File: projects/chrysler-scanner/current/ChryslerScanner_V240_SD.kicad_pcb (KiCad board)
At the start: 4 copper layers, 110 x 55 mm, 281 parts, among them J1 226A-1202, J2 USB-C, J3 I2C, J4 microSD / DM3AT-SF-PEJM5, Q1 CJ3439KDW, Q10 DMC3071LVT-7, Q11 DMC3071LVT-7, Q12 DMG6601LVT-7, Q13 DMG6601LVT-7, Q14 DMG6601LVT-7, Q15 DMG6601LVT-7, Q16 CJ3439KDW, Q17 AO3400, Q18 AO3400, Q19 AO3400, Q2 2N7002DW, Q20 AO3400, Q3 2N7002DW, Q4 2N7002DW, Q5 UMH3N, Q6 CJ3439KDW, Q7 HSSK8811, Q8 DMC3071LVT-7, Q9 DMC3071LVT-7, SW1 RESET, SW2 BOOT, SW3 LOG / SAFE STOP, U1 SY6283, U10 ESP32-PICO-V3-02, U11 USBLC6-2SC6, U12 CP2102, U13 74LVC2G66, U14 74LVC2G66, U15 74LVC2G66, U16 TS391C, U17 74LVC1G17, U18 74LVC1G14, U19 AW9523B, U2 LMR14010, U20 MCP1825S-3302E/DB, U21 TMUX1511PWR, U22 LTC6993HS6-2#TRMPBF, U23 SN74LVC1G11DBVR, U24 TLV803EA30DBZR, U3 TLV76750DRV, U4 TLV76733DRV, U5 LGS6302, U6 LMR14010, U7 LMR14010, U8 TLV76701DRV, U9 TS391C

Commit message: Add hook test points and mapped debug access with verified fabrication outputs
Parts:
- added TP1: J1962-16, footprints:TestPoint_Keystone_5015_Micro_Mini, F.Cu at (107.8, 143.6)
- added TP10: PCI_VCC, footprints:TestPoint_Keystone_5015_Micro_Mini, B.Cu at (119.5, 126.1)
- added TP11: J1962-2, footprints:TestPoint_Keystone_5015_Micro_Mini, B.Cu at (114.8, 119.3)
- added TP12: J1962-3, footprints:TestPoint_Keystone_5015_Micro_Mini, B.Cu at (119.5, 116.3)
- added TP13: J1962-11, footprints:TestPoint_Keystone_5015_Micro_Mini, B.Cu at (115.3, 115.2)
- added TP14: J1962-6, footprints:TestPoint_Keystone_5015_Micro_Mini, B.Cu at (142.7, 130.9)
- added TP15: J1962-12, footprints:TestPoint_Keystone_5015_Micro_Mini, B.Cu at (118.4, 138.3)
- added TP16: J1962-14, footprints:TestPoint_Keystone_5015_Micro_Mini, B.Cu at (163.0, 152.0)
- added TP17: J1962-9, footprints:TestPoint_Keystone_5015_Micro_Mini, F.Cu at (140.4, 142.8)
- added TP18: J1962-7, footprints:TestPoint_Keystone_5015_Micro_Mini, B.Cu at (128.8, 147.5)
- added TP19: J1962-15, footprints:TestPoint_Keystone_5015_Micro_Mini, B.Cu at (125.0, 150.4)
- added TP2: +12V, footprints:TestPoint_Keystone_5015_Micro_Mini, B.Cu at (110.6, 135.0)
- added TP20: TX0, footprints:TestPoint_Keystone_5015_Micro_Mini, B.Cu at (198.6, 119.3)
- added TP21: RX0, footprints:TestPoint_Keystone_5015_Micro_Mini, F.Cu at (187.5, 121.1)
- added TP22: EN, footprints:TestPoint_Keystone_5015_Micro_Mini, B.Cu at (157.2, 104.8)
- added TP23: IO0, footprints:TestPoint_Keystone_5015_Micro_Mini, F.Cu at (186.6, 149.7)
- added TP24: SCL, footprints:TestPoint_Keystone_5015_Micro_Mini, B.Cu at (175.3, 143.8)
- added TP25: SDA, footprints:TestPoint_Keystone_5015_Micro_Mini, F.Cu at (162.8, 118.6)
- added TP26: PCI_RX, footprints:TestPoint_Keystone_5015_Micro_Mini, B.Cu at (131.3, 121.0)
- added TP27: PCI_TX, footprints:TestPoint_Keystone_5015_Micro_Mini, B.Cu at (161.9, 125.8)
- added TP28: RX1, footprints:TestPoint_Keystone_5015_Micro_Mini, B.Cu at (171.5, 106.6)
- added TP29: TX1, footprints:TestPoint_Keystone_5015_Micro_Mini, B.Cu at (130.9, 104.4)
- added TP3: VBUS, footprints:TestPoint_Keystone_5015_Micro_Mini, B.Cu at (204.1, 110.5)
- added TP30: RX2, footprints:TestPoint_Keystone_5015_Micro_Mini, B.Cu at (136.1, 146.9)
- added TP31: TX2, footprints:TestPoint_Keystone_5015_Micro_Mini, B.Cu at (124.1, 139.2)
- added TP32: ACT_LED, footprints:TestPoint_Keystone_5015_Micro_Mini, B.Cu at (183.3, 122.3)
- added TP33: HEARTBEAT_VALID, footprints:TestPoint_Keystone_5015_Micro_Mini, B.Cu at (161.8, 105.0)
- added TP34: LOGIC_PG, footprints:TestPoint_Keystone_5015_Micro_Mini, B.Cu at (162.5, 145.8)
- added TP35: N_R88_2, footprints:TestPoint_Keystone_5015_Micro_Mini, B.Cu at (152.9, 126.7)
- added TP36: V_BA_PRE, footprints:TestPoint_Keystone_5015_Micro_Mini, B.Cu at (144.2, 113.2)
- added TP37: V_BA, footprints:TestPoint_Keystone_5015_Micro_Mini, B.Cu at (146.4, 126.7)
- added TP38: V_BT_PRE, footprints:TestPoint_Keystone_5015_Micro_Mini, B.Cu at (171.7, 129.1)
- added TP39: V_BT, footprints:TestPoint_Keystone_5015_Micro_Mini, B.Cu at (154.3, 150.6)
- added TP4: +5V, footprints:TestPoint_Keystone_5015_Micro_Mini, F.Cu at (130.1, 117.6)
- added TP40: V_PR_PRE, footprints:TestPoint_Keystone_5015_Micro_Mini, B.Cu at (139.3, 112.9)
- added TP41: V_PR, footprints:TestPoint_Keystone_5015_Micro_Mini, B.Cu at (167.0, 130.5)
- added TP42: SD_DETECT, footprints:TestPoint_Keystone_5015_Micro_Mini, F.Cu at (195.7, 139.3)
- added TP43: CCD+, footprints:TestPoint_Keystone_5015_Micro_Mini, F.Cu at (129.8, 112.8)
- added TP44: CCD-, footprints:TestPoint_Keystone_5015_Micro_Mini, B.Cu at (121.2, 111.8)
- added TP45: SD_CS, footprints:TestPoint_Pad_D1.0mm, B.Cu at (181.6, 133.3)
- added TP46: SD_SCK, footprints:TestPoint_Pad_D1.0mm, F.Cu at (191.6, 139.3)
- added TP47: SD_MOSI, footprints:TestPoint_Pad_D1.0mm, B.Cu at (184.4, 131.0)
- added TP48: SD_MISO, footprints:TestPoint_Pad_D1.0mm, B.Cu at (187.5, 113.4)
- added TP49: GND, footprints:TestPoint_Keystone_5015_Micro_Mini, B.Cu at (115.2, 143.0)
- added TP5: +3.3V, footprints:TestPoint_Keystone_5015_Micro_Mini, B.Cu at (159.9, 131.9)
- added TP50: GND, footprints:TestPoint_Keystone_5015_Micro_Mini, B.Cu at (134.4, 152.2)
- added TP51: GND, footprints:TestPoint_Keystone_5015_Micro_Mini, B.Cu at (169.3, 145.2)
- added TP52: GND, footprints:TestPoint_Keystone_5015_Micro_Mini, B.Cu at (204.0, 114.4)
- added TP6: SD_3V3, footprints:TestPoint_Keystone_5015_Micro_Mini, B.Cu at (199.0, 134.6)
- added TP7: +7.5V, footprints:TestPoint_Keystone_5015_Micro_Mini, B.Cu at (197.2, 112.1)
- added TP8: VBB, footprints:TestPoint_Keystone_5015_Micro_Mini, B.Cu at (138.3, 126.7)
- added TP9: VPP, footprints:TestPoint_Keystone_5015_Micro_Mini, F.Cu at (149.6, 125.9)
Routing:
- net TX0: track 2.43 -> 8.13 mm, vias 0 -> 1
- net SD_MOSI: track 29.4 -> 34.8 mm, vias 2 -> 3
- net HEARTBEAT_VALID: track 12.9 -> 18.1 mm, vias 2 -> 3
- net V_PR_PRE: track 60.3 -> 65.3 mm
- net IO0: track 56.6 -> 60.6 mm
- net SD_3V3: track 27.5 -> 30.5 mm
- net SCL: track 59.5 -> 62.5 mm
- net CCD+: track 8.68 -> 11.7 mm
- net SDA: track 53.3 -> 55.6 mm
- net J1962-14: track 105.5 -> 107.7 mm
- net J1962-16: track 12.6 -> 14.9 mm
- net VBUS: track 41.5 -> 42.2 mm
- net PCI_TX: track 66.2 -> 66.9 mm
- net J1962-2: track 41.6 -> 42.4 mm
- net RX0: track 42.1 -> 42.9 mm
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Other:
- board text added: "TP1"
- board text added: "TP10"
- board text added: "TP11"
- board text added: "TP12"
- board text added: "TP13"
- board text added: "TP14"
- board text added: "TP15"
- board text added: "TP16"
- board text added: "TP17"
- board text added: "TP18"
- board text added: "TP19"
- board text added: "TP2"
- board text added: "TP20"
- board text added: "TP21"
- board text added: "TP22"
- board text added: "TP23"
- board text added: "TP24"
- board text added: "TP25"
- board text added: "TP26"
- board text added: "TP27"
- board text added: "TP28"
- board text added: "TP29"
- board text added: "TP3"
- board text added: "TP30"
- board text added: "TP31"
- board text added: "TP32"
- board text added: "TP33"
- board text added: "TP34"
- board text added: "TP35"
- board text added: "TP36"
- board text added: "TP37"
- board text added: "TP38"
- board text added: "TP39"
- board text added: "TP4"
- board text added: "TP40"
- board text added: "TP41"
- board text added: "TP42"
- board text added: "TP43"
- board text added: "TP44"
- board text added: "TP45"
- board text added: "TP46"
- board text added: "TP47"
- board text added: "TP48"
- board text added: "TP49"
- board text added: "TP5"
- board text added: "TP50"
- board text added: "TP51"
- board text added: "TP52"
- board text added: "TP6"
- board text added: "TP7"
- board text added: "TP8"
- board text added: "TP9"

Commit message: Finish Chrysler scanner CCD correction and procurement fabrication package
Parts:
- C14: footprint footprints:C_1206_3216Metric -> footprints:C_1210_3225_TDK_22u50V
- D11, D15, D16, D17, D18, D19, D20, D21, D22: value MSK4005 -> PMEG4005
- D12, D13, D14: value ESD5Z12V -> SMF12A
- D27, D28, D29: value ESD5Z3V3 -> PESD3V3U1UA
- L1, L2, L4, L6: footprint footprints:L_7.3x7.3_H3.5 -> footprints:L_Eaton_DR74_220_R
- L3, L5: footprint footprints:R_1206_3216Metric -> footprints:L_Bourns_SRN2012
- Q1, Q16, Q6, Q7: footprint footprints:SOT-23-6 -> footprints:SOT-363_SC-70-6_RR
- Q2, Q3, Q4: value 2N7002DW -> DMN62D2UDM
- R98, R99: value 100Ω -> 330Ω
- U17: value 74LVC1G17 -> 74AHCT1G17GV
- U18: value 74LVC1G14 -> SN74AHCT1G14
- moved C14 2.76 mm to (157.8, 116.5)
- moved L3 2.69 mm to (150.9, 121.2)
- moved L5 2.24 mm to (163.0, 139.2), turned to 0 degrees
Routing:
- net VPP: track 109.5 -> 115.0 mm
- net VBB: track 112.6 -> 117.8 mm
- net N_R8_1: track 21.6 -> 26.2 mm
- net GND: track 403.9 -> 405.5 mm
- net 4: track 0.00 -> 1.06 mm
- net RX7_BIAS_EN: track 52.3 -> 53.1 mm
- net 30: track 0.00 -> 0.71 mm
- net 64: track 0.00 -> 0.54 mm
- net 31: track 0.00 -> 0.54 mm

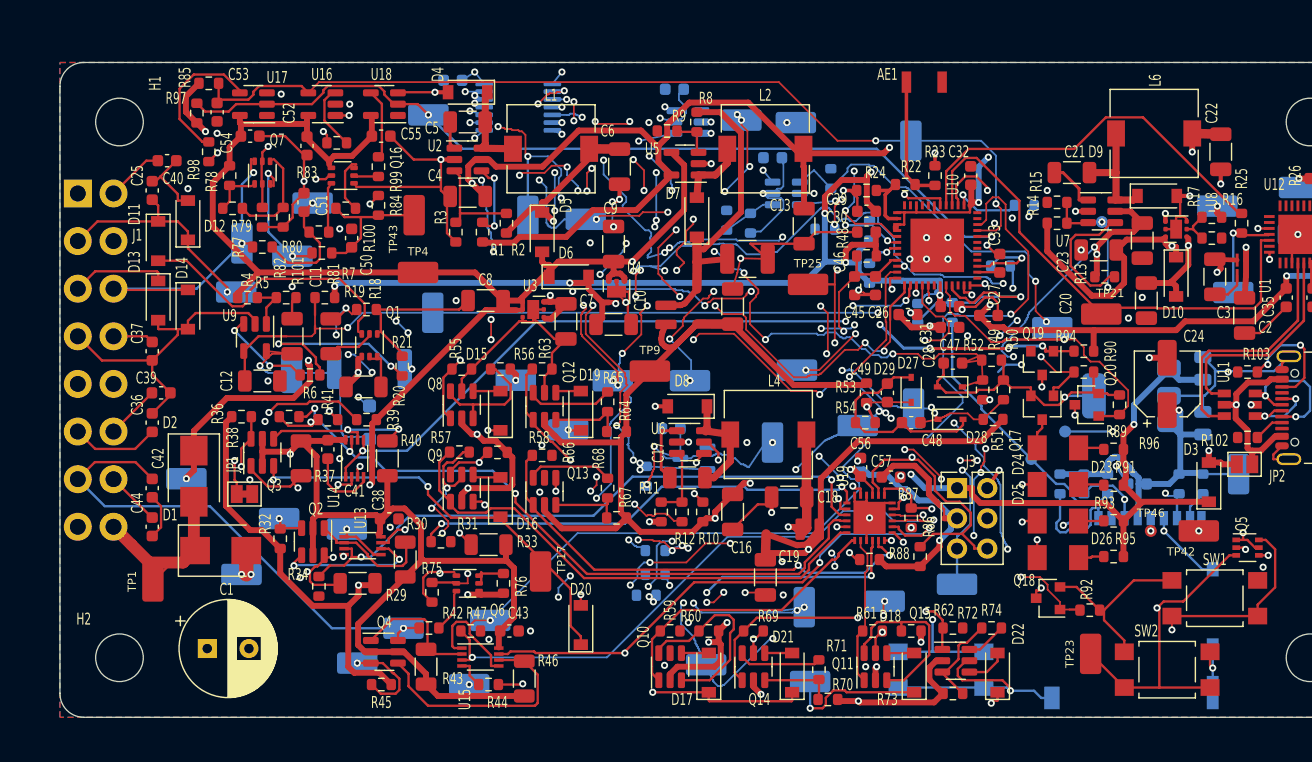
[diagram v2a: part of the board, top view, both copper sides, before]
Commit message: Refine programming drive, Eaton lands and mounting clearance
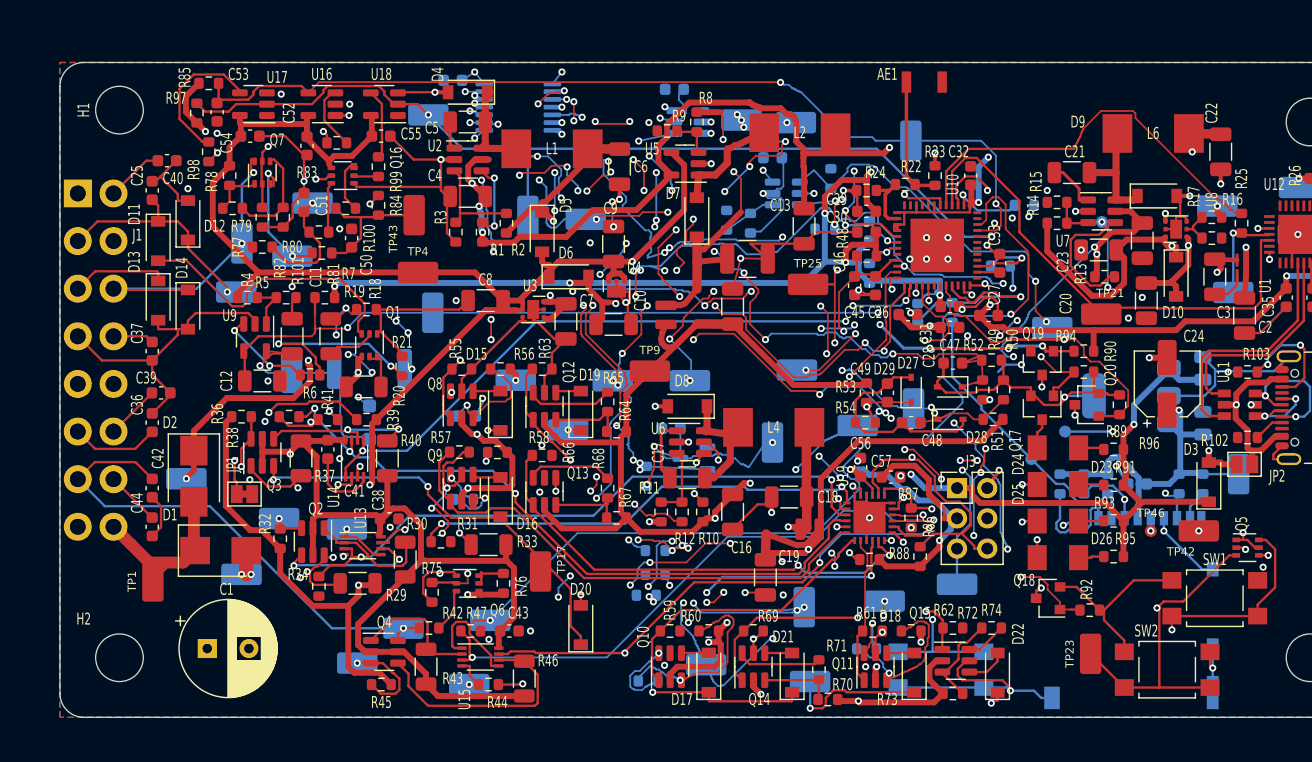
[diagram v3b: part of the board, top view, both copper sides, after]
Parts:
- added R124: 8.2k 1%, footprints:R_0603_1608Metric, B.Cu at (134.2, 129.7)
- added R125: 8.2k 1%, footprints:R_0603_1608Metric, B.Cu at (133.9, 136.7)
- added R126: 8.2k 1%, footprints:R_0603_1608Metric, B.Cu at (149.4, 151.9)
- added R127: 8.2k 1%, footprints:R_0603_1608Metric, B.Cu at (167.8, 149.2)
- L1, L2, L4, L6: footprint footprints:L_Eaton_DR74_220_R -> footprints:L_Eaton_DR74_Recommended
- Q10, Q11, Q8, Q9: value DMC3071LVT-7 -> DMG6601LVT-7
- moved L2 3.20 mm to (162.2, 105.9)
- moved H1 1.00 mm to (105.0, 104.0)
- moved L4 0.75 mm to (159.9, 130.7)
- moved L1 0.08 mm to (141.3, 107.2)
- moved L6 0.08 mm to (191.8, 106.0)
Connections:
- Q10 pad 6: N_R60_2 -> N_R126_1
- Q11 pad 6: N_R62_2 -> N_R127_1
- Q8 pad 6: N_R56_2 -> N_R124_1
- Q9 pad 6: N_R58_2 -> N_R125_1
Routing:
- net +12V: track 186.5 -> 175.2 mm, vias 11 -> 13
- net N_R126_1: track 0.00 -> 6.84 mm, vias 0 -> 1
- net EN: track 101.8 -> 107.0 mm, vias 10 -> 12
- net N_R127_1: track 0.00 -> 5.05 mm, vias 0 -> 1
- net N_R124_1: track 0.00 -> 4.65 mm, vias 0 -> 2
- net N_D7_2: track 6.64 -> 10.3 mm
- net N_R125_1: track 0.00 -> 3.09 mm, vias 0 -> 1
- net V_BA: track 94.2 -> 96.5 mm
- net V_PR_PRE: track 65.3 -> 67.2 mm
- net N_R25_1: track 32.9 -> 34.1 mm
- net N_R62_2: track 15.2 -> 14.1 mm, vias 0 -> 1
- net GND: track 405.5 -> 406.6 mm, vias 99 -> 98
- net 4: track 1.06 -> 0.00 mm
- net V_BT_PRE: track 61.3 -> 62.2 mm
- net +5V: track 245.1 -> 245.8 mm
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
